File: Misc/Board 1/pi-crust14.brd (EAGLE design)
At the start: 101.6 x 78.8 mm, 35 parts, among them IC3 74LS595D, IC4 74LS595D, IC5 74LS595D, IC6 74LS595D, U1 AD9983AKSTZ_140, U2 SN54LS253_J_16, U3 SN54LS253_J_16, U4 SN54LS253_J_16

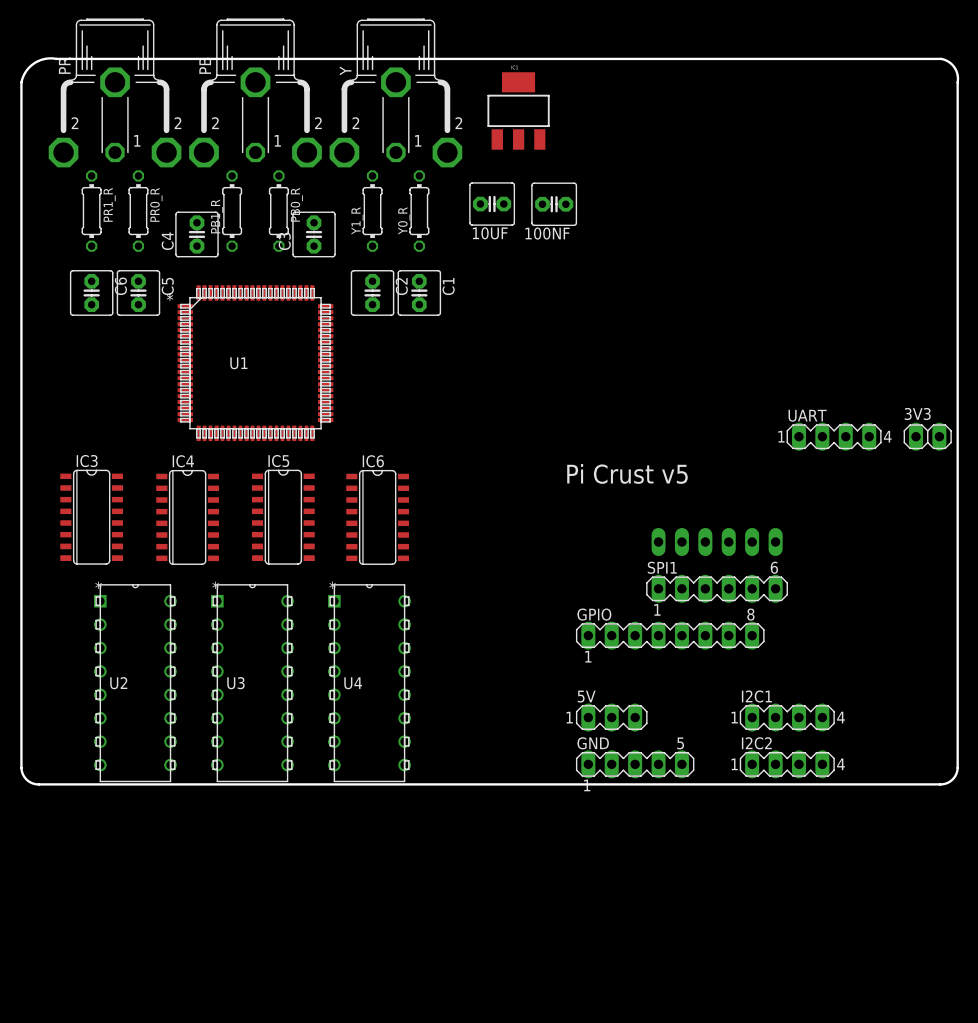
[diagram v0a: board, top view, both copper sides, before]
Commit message: Board Update 2
DFF implemented, working on and gates and binary counter
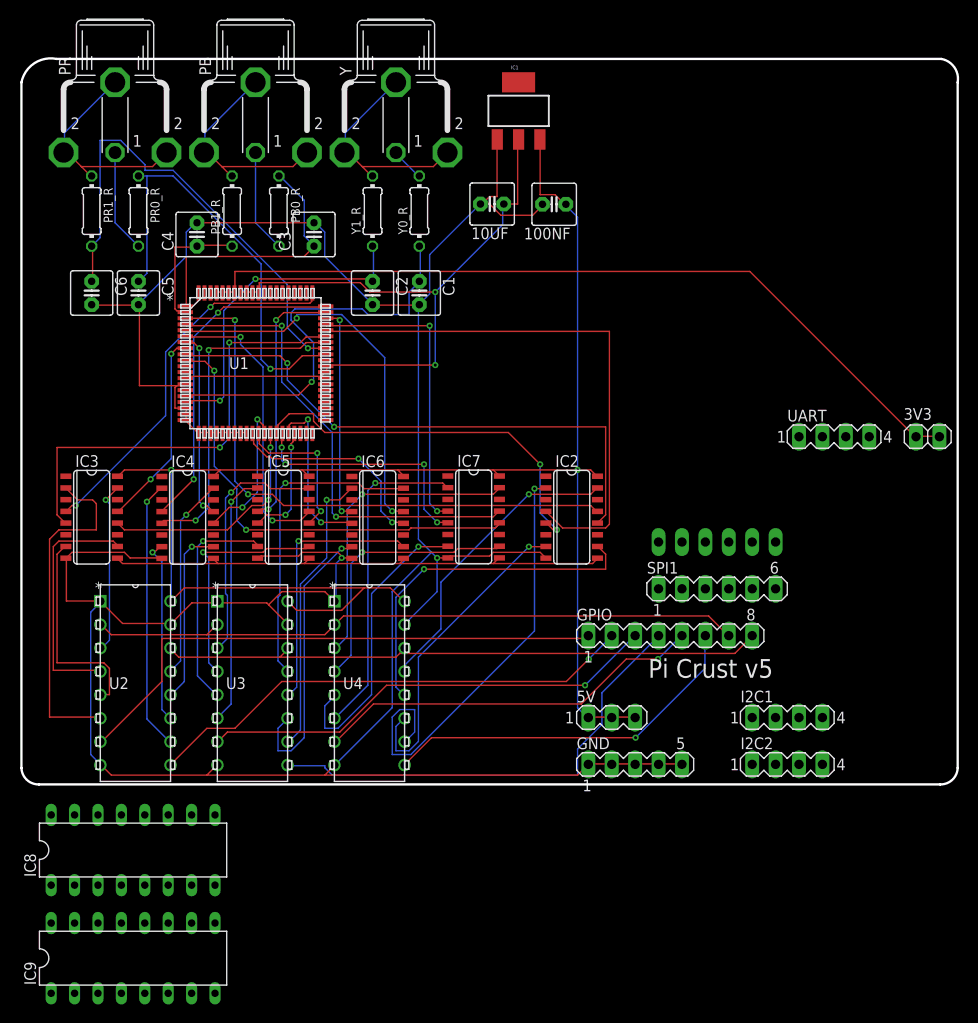
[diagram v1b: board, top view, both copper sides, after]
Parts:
- added IC2, IC7: 74LS595D, SparkFun-DigitalIC:SO16
- added IC8, IC9: 74AC11008, 74ac-logic:DIL16
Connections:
- new net B0: IC2.13, U1.61
- new net B0_OUT: IC2.15, U4.13
- new net B1: IC7.13, U1.60
- new net B1_OUT: IC7.15, U4.3
- new net B2_OUT: IC6.15, U3.13
- new net B3_OUT: IC5.15, U3.3
- new net B6_OUT: IC2.10, U4.12
- new net B7_OUT: IC7.10, U4.4
- new net G0: IC6.12, U1.49
- new net G0_OUT: IC6.10, U3.12
- new net G1: IC5.12, U1.48
- new net G1_OUT: IC5.10, U3.4
- new net G4_OUT: IC2.7, U4.11
- new net G5_OUT: IC7.7, U4.5
- new net G6_OUT: IC6.7, U3.11
- new net G7_OUT: IC5.7, U3.5
- new net R2_0UT: IC2.2, U4.10
- new net R3_OUT: IC7.2, U4.6
- new net R4_OUT: IC6.2, U3.10
- net 5V: now also IC2.1, IC2.16, IC3.1, IC3.16, IC4.1, IC4.16, IC5.1, IC5.16, IC6.1, IC6.16, IC7.1, IC7.16
- net B2: now also IC6.13; no longer U2.4
- net B3: now also IC5.13; no longer U2.12
- net B4: no longer U3.4
- net B4_OUT: now also U2.13
- net B5: no longer U3.12
- net B5_OUT: now also U2.3
- net B6: now also IC2.12; no longer U4.4
- net B7: now also IC7.12; no longer U4.12
- net CLK: now also IC2.9, IC5.9, IC6.9, IC7.9
- net G2: no longer U2.5
- net G2_OUT: now also U2.12
- net G3: no longer U2.11
- net G3_OUT: now also U2.4
- net G4: now also IC2.5; no longer U3.5
- net G5: now also IC7.5; no longer U3.11
- net G6: now also IC6.5; no longer U4.5
- net G7: now also IC5.5; no longer U4.11
- net GND: now also IC8.4, IC8.5, IC9.4, IC9.5; no longer IC6.8
- net GND_WIRE: now also IC2.8, IC6.8, IC7.8, U1.72; no longer U2.13, U2.3, U3.13, U3.3, U4.13, U4.3
- net R0_OUT: now also U2.11
- net R1_OUT: now also U2.5
- net R2: now also IC2.4; no longer U2.6
- net R3: now also IC7.4; no longer U2.10
- net R4: now also IC6.4; no longer U3.6
- net R5: now also IC5.4; no longer U3.10
- net R5_OUT: now also U3.6
- net R6: no longer U4.6
- net R6_OUT: now also U2.10
- net R7: no longer U4.10
- net R7_OUT: now also U2.6
- net VCC: now also IC8.12, IC8.13, IC9.12, IC9.13; no longer IC3.16, IC4.16, IC5.16, IC6.16
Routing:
- net GND_WIRE: track 0.00 -> 333.2 mm, vias 0 -> 2
- net 5V: track 0.00 -> 178.3 mm, vias 0 -> 2
- net 3V3: track 0.00 -> 88.4 mm
- net 1.8V: track 0.00 -> 81.4 mm, vias 0 -> 2
- net S1: track 0.00 -> 71.9 mm
- net S0: track 0.00 -> 66.7 mm
- net B0: track 0.00 -> 63.6 mm, vias 0 -> 2
- net B6: track 0.00 -> 60.8 mm, vias 0 -> 2
- net MSB1: track 0.00 -> 60.4 mm
- net R2: track 0.00 -> 59.6 mm
- net CLK: track 0.00 -> 55.8 mm
- net MSB2: track 0.00 -> 53.7 mm, vias 0 -> 1
- net RIN1_ADC: track 0.00 -> 52.7 mm, vias 0 -> 1
- net B1: track 0.00 -> 51.7 mm, vias 0 -> 2
- net MSB4: track 0.00 -> 50.8 mm
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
